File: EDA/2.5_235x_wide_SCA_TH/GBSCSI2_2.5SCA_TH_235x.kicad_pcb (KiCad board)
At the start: 4 copper layers, 69.5 x 93.5 mm, 145 parts, among them J1 SCSI_50-2P_2mm, J1.1 SCSI_50P_2.54mm, J2 TF003, J3 GCT-4105, J4 SM03B-SRSS-TB, J4.1 Conn_01x04, J5 Conn_01x04, J6 Conn_01x02, Q1 AO3401A, Q10 AO3401A, Q11 AO3401A, Q12 AO3401A, Q13 AO3401A, Q14 AO3401A, Q15 AO3401A, Q16 AO3401A, Q17 AO3401A, Q18 AO3401A, Q2 AO3401A, Q3 AO3401A, Q4 AO3401A, Q5 AO3401A, Q6 AO3401A, Q7 AO3401A, Q8 AO3401A, Q9 AO3401A, SW1 SW_DIP_x04, U1 RP2350_60QFN, U10 AZ1117-2.85, U2 W25Q128JVS, U3 USB TVS, U4 74LVTH245, U5 74LVTH245, U6 74LVTH125, U7 74LVTH125, U8 SN74AHC1G125DBVR, U9 TLV62569DBV, Y1 12MHz

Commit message: SCA variant mostly laid out
Or rather, a first pass.
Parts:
- removed C24, C32, C33: 100nF, Capacitor_SMD:C_0603_1608Metric
- removed C31, C34: 1μF, Capacitor_SMD:C_0603_1608Metric
- removed D1, D3, D4: 1N5819, Diode_SMD:D_SOD-123
- removed F1: 1A, Fuse:Fuse_0805_2012Metric
- removed J1.1: SCSI_50P_2.54mm, Connector_IDC:IDC-Header_2x25_P2.54mm_Horizontal
- removed J5: Conn_01x04, Connector_PinHeader_2.54mm:PinHeader_1x04_P2.54mm_Horizontal
- removed JP1: Jumper_2_Open, Connector_PinHeader_2.54mm:PinHeader_2x01_P2.54mm_Vertical
- removed Q1, Q10, Q11, Q12, Q13, Q14, Q15, Q16, Q17, Q18, Q2, Q3, Q4, Q5, Q6, Q7, Q8, Q9: AO3401A, Package_TO_SOT_SMD:SOT-23
- removed R11, R12, R29, R5, R7: 4.7kΩ, Resistor_SMD:R_0603_1608Metric
- removed R17, R27: 1kΩ, Resistor_SMD:R_0603_1608Metric
- removed R31, R32, R33, R34, R35, R36, R37, R38, R39, R40, R41, R42, R43, R44, R45, R46, R47, R48: 110Ω, Resistor_SMD:R_0603_1608Metric
- removed R52: 0Ω, Resistor_SMD:R_0603_1608Metric
- removed R53: ~, Resistor_SMD:R_0603_1608Metric
- removed SW1: SW_DIP_x04, Button_Switch_SMD:SW_DIP_SPSTx04_Slide_6.7x11.72mm_W8.61mm_P2.54mm_LowProfile
- removed U10: AZ1117-2.85, Package_TO_SOT_SMD:SOT-223-3_TabPin2
- removed U8: SN74AHC1G125DBVR, Package_TO_SOT_SMD:SOT-23-5
- added C15: 100nF, Capacitor_SMD:C_0402_1005Metric, F.Cu at (53.0, 110.8)
- added C36: 100nF, Capacitor_SMD:C_0402_1005Metric, F.Cu at (67.5, 111.8)
- added C37: 4.7μF, Capacitor_SMD:C_0402_1005Metric, F.Cu at (82.5, 97.1)
- added C38: 100nF, Capacitor_SMD:C_0402_1005Metric, F.Cu at (89.0, 100.2)
- added C39: 10μF, Capacitor_SMD:C_0603_1608Metric, F.Cu at (89.0, 103.2)
- added C40: 10μF, Capacitor_SMD:C_0603_1608Metric, F.Cu at (89.0, 101.8)
- added C41: 100nF, Capacitor_SMD:C_0603_1608Metric, F.Cu at (48.5, 84.5)
- added C42: 100nF, Capacitor_SMD:C_0402_1005Metric, F.Cu at (68.8, 79.5)
- added J8: Conn_01x02, Connector_PinHeader_2.54mm:PinHeader_1x02_P2.54mm_Vertical, F.Cu at (79.5, 116.2)
- added L3: 1μH, Inductor_SMD:L_1008_2520Metric, F.Cu at (89.2, 97.8)
- added R57: 4.7kΩ, Resistor_SMD:R_0603_1608Metric, F.Cu at (54.1, 84.5)
- added R58: 4.7kΩ, Resistor_SMD:R_0603_1608Metric, F.Cu at (84.0, 90.2)
- added R59: 4.7kΩ, Resistor_SMD:R_0603_1608Metric, F.Cu at (67.0, 84.5)
- added R60: 10kΩ, Resistor_SMD:R_0402_1005Metric, F.Cu at (86.0, 101.2)
- added R61: 374kΩ, Resistor_SMD:R_0402_1005Metric, F.Cu at (86.0, 103.2)
- added R62: 100kΩ, Resistor_SMD:R_0402_1005Metric, F.Cu at (86.0, 102.2)
- added R63: 10k, Resistor_SMD:R_0603_1608Metric, F.Cu at (53.2, 56.2)
- added R66: 4.7kΩ, Resistor_SMD:R_0603_1608Metric, F.Cu at (98.0, 140.5)
- added R67: 10k, Resistor_SMD:R_0603_1608Metric, F.Cu at (91.2, 56.2)
- added R68: 4.7kΩ, Resistor_SMD:R_0402_1005Metric, F.Cu at (49.5, 103.0)
- added R69: 4.7kΩ, Resistor_SMD:R_0402_1005Metric, F.Cu at (49.5, 105.0)
- added R70: 4.7kΩ, Resistor_SMD:R_0402_1005Metric, F.Cu at (49.5, 107.0)
- added SW2: SW_DIP_x03, Button_Switch_SMD:SW_DIP_SPSTx03_Slide_6.7x9.18mm_W8.61mm_P2.54mm_LowProfile, F.Cu at (96.2, 132.5)
- added SW3: GT-TC108A-H034-L1S, Button_Switch_SMD:SW_Push_1P1T-MP_NO_Horizontal_Alps_SKRTLAE010, F.Cu at (94.2, 140.5)
- added U11: TLV62569DBV, Package_TO_SOT_SMD:SOT-23-5, F.Cu at (85.2, 97.5)
- added U12: 74LVTH245, Package_SO:SSOP-20_5.3x7.2mm_P0.65mm, F.Cu at (45.2, 89.2)
- C10: value 4.7uF -> 4.7μF
- C20, C35: value 47uF -> 47μF
- J1: value SCSI_50-2P_2mm -> Conn_02x40_Counter_Clockwise; footprint GBSCSI:PinHeader_2x25-2_P2.00mm_straddle -> GBSCSI:CHAMPII_80; moved to B.Cu
- U1: value RP2350_60QFN -> RP2350_80QFN; footprint Package_DFN_QFN:QFN-60-1EP_7x7mm_P0.4mm_EP3.4x3.4mm_ThermalVias -> GBSCSI:RP2350-QFN-80-1EP_10x10_P0.4mm_EP3.4x3.4mm_ThermalVias
- moved D2 52.3 mm to (135.3, 96.8)
- moved F2 52.3 mm to (135.0, 99.1)
- moved REF** 38.8 mm to (56.5, 78.9)
- moved C20 17.7 mm to (80.0, 100.8), turned to 180 degrees
- moved C35 15.3 mm to (80.0, 103.2), turned to 180 degrees
- moved J1 13.8 mm to (70.3, 62.5), turned to 0 degrees
- moved R28 9.37 mm to (76.2, 84.5)
- moved R8 7.12 mm to (73.8, 85.2), turned to -90 degrees
- moved R30 7.04 mm to (73.8, 91.1)
- moved R25 6.64 mm to (84.0, 87.0)
- moved U4 6.57 mm to (56.5, 89.2)
- moved U6 6.57 mm to (69.0, 89.2)
- moved R26 6.55 mm to (95.4, 88.5)
- moved R6 6.55 mm to (96.0, 86.2)
- moved U5 6.55 mm to (89.8, 89.2)
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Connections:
- C22 pad 1: +3.3V -> +2.8V
- C23 pad 1: +3.3V -> +2.8V
- C25 pad 1: +3.3V -> +2.8V
- C26 pad 1: +3.3V -> +2.8V
- J1 pad 1: +5VIN -> unconnected-(J1-Pin_1-Pad1)
- J1 pad 10: /Host Interface/~{SCSI_SD2} -> /Host Interface/~{SCSI_SD8}
- J1 pad 11: GND -> /Host Interface/SCSI_I/~{O}
- J1 pad 12: /Host Interface/~{SCSI_SD3} -> /Host Interface/SCSI_~{REQ}
- J1 pad 13: GND -> /Host Interface/SCSI_~{C}/D
- J1 pad 14: /Host Interface/~{SCSI_SD4} -> /Host Interface/~{SCSI_SEL}
- J1 pad 15: GND -> /Host Interface/~{SCSI_MSG}
- J1 pad 16: /Host Interface/~{SCSI_SD5} -> /Host Interface/~{SCSI_RST}
- J1 pad 18: /Host Interface/~{SCSI_SD6} -> /Host Interface/~{SCSI_BSY}
- J1 pad 19: GND -> /Host Interface/SCSI_~{ATTN}
- J1 pad 2: +5VIN -> unconnected-(J1-Pin_2-Pad2)
- J1 pad 20: /Host Interface/~{SCSI_SD7} -> /Host Interface/~{SCSI_SDP}
- J1 pad 21: GND -> /Host Interface/~{SCSI_SD7}
- J1 pad 22: /Host Interface/~{SCSI_SDP} -> /Host Interface/~{SCSI_SD6}
- J1 pad 23: GND -> /Host Interface/~{SCSI_SD5}
- J1 pad 24: +5VTT -> /Host Interface/~{SCSI_SD4}
- J1 pad 25: /Host Interface/SCSI_~{ATTN} -> /Host Interface/~{SCSI_SD3}
- J1 pad 26: /Host Interface/~{SCSI_BSY} -> /Host Interface/~{SCSI_SD2}
- J1 pad 27: GND -> /Host Interface/~{SCSI_SD1}
- J1 pad 28: /Host Interface/~{SCSI_ACK} -> /Host Interface/~{SCSI_SD0}
- J1 pad 29: /Host Interface/~{SCSI_RST} -> /Host Interface/~{SCSI_SDP1}
- J1 pad 3: GND -> unconnected-(J1-Pin_3-Pad3)
- J1 pad 30: /Host Interface/~{SCSI_MSG} -> /Host Interface/~{SCSI_SD15}
- J1 pad 31: GND -> /Host Interface/~{SCSI_SD14}
- J1 pad 32: /Host Interface/~{SCSI_SEL} -> /Host Interface/~{SCSI_SD13}
- J1 pad 33: /Host Interface/SCSI_I/~{O} -> /Host Interface/~{SCSI_SD12}
- J1 pad 34: /Host Interface/SCSI_~{C}/D -> +5VIN
- J1 pad 35: GND -> +5VIN
- J1 pad 36: /Host Interface/SCSI_~{REQ} -> +5VIN
- J1 pad 37: GND -> unconnected-(J1-Pin_37-Pad37)
- J1 pad 38: GND -> unconnected-(J1-Pin_38-Pad38)
- J1 pad 39: +5VIN -> unconnected-(J1-Pin_39-Pad39)
- J1 pad 4: GND -> unconnected-(J1-Pin_4-Pad4)
- J1 pad 40: +5VIN -> unconnected-(J1-Pin_40-Pad40)
- J1 pad 43: unconnected-(J1-Pin_43-Pad43) -> GND
- J1 pad 44: unconnected-(J1-Pin_44-Pad44) -> Net-(J1-Pin_44)
- J1 pad 46: unconnected-(J1-Pin_46-Pad46) -> GND
- J1 pad 47: unconnected-(J1-Pin_47-Pad47) -> GND
- J1 pad 48: unconnected-(J1-Pin_48-Pad48) -> GND
- J1 pad 49: unconnected-(J1-Pin_49-Pad49) -> GND
- J1 pad 5: GND -> unconnected-(J1-Pin_5-Pad5)
- J1 pad 50: unconnected-(J1-Pin_50-Pad50) -> GND
- J1 pad 6: /Host Interface/~{SCSI_SD0} -> unconnected-(J1-Pin_6-Pad6)
- J1 pad 7: GND -> /Host Interface/~{SCSI_SD11}
- J1 pad 8: /Host Interface/~{SCSI_SD1} -> /Host Interface/~{SCSI_SD10}
- J1 pad 9: GND -> /Host Interface/~{SCSI_SD9}
- R10 pad 1: /Core Logic, Basic Controls/~{DEBUG} -> Net-(R10-Pad1)
- R10 pad 2: /Core Logic, Basic Controls/~{MCU_REQ} -> /Core Logic, Basic Controls/~{DEBUG}
- R13 pad 2: /Core Logic, Basic Controls/~{DEBUG} -> Net-(R10-Pad1)
- R6 pad 1: +3.3V -> +2.8V
- R8 pad 1: +3.3V -> +2.8V
- R9 pad 2: /Core Logic, Basic Controls/~{MCU_ATTN} -> /Core Logic, Basic Controls/~{MCU_ACK}
- U1 pad 1: +3.3V -> /Core Logic, Basic Controls/~{MCU_SD0}
- U1 pad 10: /Core Logic, Basic Controls/~{MCU_SD7} -> +1.1V
- U1 pad 11: +3.3V -> /Core Logic, Basic Controls/~{MCU_SD8}
- U1 pad 12: /Core Logic, Basic Controls/~{MCU_SDP} -> /Core Logic, Basic Controls/~{MCU_SD9}
- U1 pad 13: /Core Logic, Basic Controls/~{BUS_DIR} -> /Core Logic, Basic Controls/~{MCU_SD10}
- U1 pad 14: /Core Logic, Basic Controls/SDIO_CLK -> /Core Logic, Basic Controls/~{MCU_SD11}
- U1 pad 15: /Core Logic, Basic Controls/SDIO_CMD -> +3.3V
- U1 pad 16: /Core Logic, Basic Controls/SDIO_D0 -> /Core Logic, Basic Controls/~{MCU_SD12}
- U1 pad 17: /Core Logic, Basic Controls/SDIO_D1 -> /Core Logic, Basic Controls/~{MCU_SD13}
- U1 pad 18: /Core Logic, Basic Controls/SDIO_D2 -> /Core Logic, Basic Controls/~{MCU_SD14}
- U1 pad 19: /Core Logic, Basic Controls/SDIO_D3 -> /Core Logic, Basic Controls/~{MCU_SD15}
- U1 pad 2: /Core Logic, Basic Controls/~{MCU_SD0} -> /Core Logic, Basic Controls/~{MCU_SD1}
- U1 pad 20: +3.3V -> /Core Logic, Basic Controls/~{MCU_SDP}
- U1 pad 21: /Core Logic, Basic Controls/XIN -> /Core Logic, Basic Controls/~{MCU_SDP1}
- U1 pad 22: /Core Logic, Basic Controls/XOUT -> /Core Logic, Basic Controls/~{MCU_REQ}
- U1 pad 23: +1.1V -> /Core Logic, Basic Controls/BUS_DIR
- U1 pad 24: /Core Logic, Basic Controls/SWCLK -> +3.3V
- U1 pad 25: /Core Logic, Basic Controls/SWD -> /Core Logic, Basic Controls/~{MCU_CD/SEL_IN}
- U1 pad 26: unconnected-(U1-RUN-Pad26) -> /Core Logic, Basic Controls/~{MCU_ATTN}
- U1 pad 27: /Core Logic, Basic Controls/LED_OUT -> /Core Logic, Basic Controls/~{MCU_MSG/BSY_IN}
- U1 pad 28: /Core Logic, Basic Controls/~{MCU_REQ} -> /Core Logic, Basic Controls/~{MCU_ACK}
- U1 pad 29: /Core Logic, Basic Controls/~{MCU_CD/SEL_IN} -> +3.3V
- U1 pad 3: /Core Logic, Basic Controls/~{MCU_SD1} -> /Core Logic, Basic Controls/~{MCU_SD2}
- U1 pad 30: +3.3V -> /Core Logic, Basic Controls/XIN
- U1 pad 31: /Core Logic, Basic Controls/~{MCU_SEL_OUT} -> /Core Logic, Basic Controls/XOUT
- U1 pad 32: /Core Logic, Basic Controls/~{MCU_MSG/BSY_IN} -> +1.1V
- U1 pad 33: /Core Logic, Basic Controls/MCU_RST -> /Core Logic, Basic Controls/SWCLK
- U1 pad 34: /Core Logic, Basic Controls/~{MCU_IO} -> /Core Logic, Basic Controls/SWD
- U1 pad 35: /Core Logic, Basic Controls/~{WL_EN} -> unconnected-(U1-RUN-Pad35)
- U1 pad 36: /Core Logic, Basic Controls/WL_DAT/~{IRQ} -> /Core Logic, Basic Controls/~{MCU_IO}
- U1 pad 37: /Core Logic, Basic Controls/~{WL_CS} -> /Core Logic, Basic Controls/I²C_INT
- U1 pad 38: +3.3V -> /Core Logic, Basic Controls/I²C_SDA
- U1 pad 39: +1.1V -> /Core Logic, Basic Controls/I²C_SCL
- U1 pad 4: /Core Logic, Basic Controls/~{MCU_SD2} -> /Core Logic, Basic Controls/~{MCU_SD3}
- U1 pad 40: /Core Logic, Basic Controls/~{MCU_ACK} -> /Core Logic, Basic Controls/~{DEBUG}
- U1 pad 41: /Core Logic, Basic Controls/~{MCU_BSY_OUT} -> +3.3V
- U1 pad 42: /Core Logic, Basic Controls/~{MCU_ATTN} -> /Core Logic, Basic Controls/LED_OUT
- U1 pad 43: /Core Logic, Basic Controls/WL_SCK -> /Core Logic, Basic Controls/SDIO_CLK
- U1 pad 44: +3.3V -> /Core Logic, Basic Controls/SDIO_CMD
- U1 pad 45: +3.3V -> /Core Logic, Basic Controls/SDIO_D0
- U1 pad 46: Net-(U1-VREG_AVDD) -> /Core Logic, Basic Controls/SDIO_D1
- U1 pad 47: GND -> /Core Logic, Basic Controls/SDIO_D2
- U1 pad 48: /Core Logic, Basic Controls/VREG_LX -> /Core Logic, Basic Controls/SDIO_D3
- U1 pad 49: +3.3V -> /Core Logic, Basic Controls/~{WL_EN}
- U1 pad 5: /Core Logic, Basic Controls/~{MCU_SD3} -> +3.3V
- U1 pad 50: +1.1V -> +3.3V
- U1 pad 51: /Core Logic, Basic Controls/USB_D- -> +1.1V
- U1 pad 52: /Core Logic, Basic Controls/USB_D+ -> /Core Logic, Basic Controls/WL_DAT/~{IRQ}
- U1 pad 53: +3.3V -> /Core Logic, Basic Controls/~{WL_CS}
- U1 pad 54: +3.3V -> /Core Logic, Basic Controls/WL_SCK
- U1 pad 55: /Core Logic, Basic Controls/QSPI_SD3 -> /Core Logic, Basic Controls/EJECT
- U1 pad 56: /Core Logic, Basic Controls/QSPI_SCLK -> unconnected-(U1-GPIO45_ADC5-Pad56)
- U1 pad 57: /Core Logic, Basic Controls/QSPI_SD0 -> unconnected-(U1-GPIO46_ADC6-Pad57)
- U1 pad 58: /Core Logic, Basic Controls/QSPI_SD2 -> unconnected-(U1-GPIO47_ADC7-Pad58)
- U1 pad 59: /Core Logic, Basic Controls/QSPI_SD1 -> +3.3V
- U1 pad 6: +1.1V -> /Core Logic, Basic Controls/~{MCU_SD4}
- U1 pad 60: /Core Logic, Basic Controls/QSPI_~{SS} -> +3.3V
- U1 pad 61: GND -> Net-(U1-VREG_AVDD)
- U1 pad 7: /Core Logic, Basic Controls/~{MCU_SD4} -> /Core Logic, Basic Controls/~{MCU_SD5}
- U1 pad 8: /Core Logic, Basic Controls/~{MCU_SD5} -> /Core Logic, Basic Controls/~{MCU_SD6}
- U1 pad 9: /Core Logic, Basic Controls/~{MCU_SD6} -> /Core Logic, Basic Controls/~{MCU_SD7}
- U4 pad 1: /Core Logic, Basic Controls/~{BUS_DIR} -> /Core Logic, Basic Controls/BUS_DIR
- U4 pad 11: /Core Logic, Basic Controls/~{MCU_SD0} -> /Host Interface/~{SCSI_SD7}
- U4 pad 12: /Core Logic, Basic Controls/~{MCU_SD1} -> /Host Interface/~{SCSI_SD6}
- U4 pad 13: /Core Logic, Basic Controls/~{MCU_SD2} -> /Host Interface/~{SCSI_SD5}
- U4 pad 14: /Core Logic, Basic Controls/~{MCU_SD3} -> /Host Interface/~{SCSI_SD4}
- U4 pad 15: /Core Logic, Basic Controls/~{MCU_SD4} -> /Host Interface/~{SCSI_SD3}
- U4 pad 16: /Core Logic, Basic Controls/~{MCU_SD5} -> /Host Interface/~{SCSI_SD2}
- U4 pad 17: /Core Logic, Basic Controls/~{MCU_SD6} -> /Host Interface/~{SCSI_SD1}
- U4 pad 18: /Core Logic, Basic Controls/~{MCU_SD7} -> /Host Interface/~{SCSI_SD0}
- U4 pad 2: /Host Interface/~{SCSI_SD7} -> /Core Logic, Basic Controls/~{MCU_SD0}
- U4 pad 20: +3.3V -> +2.8V
- U4 pad 3: /Host Interface/~{SCSI_SD6} -> /Core Logic, Basic Controls/~{MCU_SD1}
- U4 pad 4: /Host Interface/~{SCSI_SD5} -> /Core Logic, Basic Controls/~{MCU_SD2}
- U4 pad 5: /Host Interface/~{SCSI_SD4} -> /Core Logic, Basic Controls/~{MCU_SD3}
- U4 pad 6: /Host Interface/~{SCSI_SD3} -> /Core Logic, Basic Controls/~{MCU_SD4}
- U4 pad 7: /Host Interface/~{SCSI_SD2} -> /Core Logic, Basic Controls/~{MCU_SD5}
- U4 pad 8: /Host Interface/~{SCSI_SD1} -> /Core Logic, Basic Controls/~{MCU_SD6}
- U4 pad 9: /Host Interface/~{SCSI_SD0} -> /Core Logic, Basic Controls/~{MCU_SD7}
- U5 pad 20: +3.3V -> +2.8V
- U6 pad 1: /Core Logic, Basic Controls/~{BUS_DIR} -> /Core Logic, Basic Controls/~{MCU_RST_OUT}
- U6 pad 14: +3.3V -> +2.8V
- U6 pad 2: /Core Logic, Basic Controls/~{MCU_SDP} -> GND
- U6 pad 3: /Host Interface/~{SCSI_SDP} -> /Host Interface/~{SCSI_RST}
- U6 pad 5: /Host Interface/~{SCSI_SDP} -> /Host Interface/~{SCSI_RST}
- U6 pad 6: Net-(R27-Pad1) -> /Core Logic, Basic Controls/~{MCU_RST_IN}
- U7 pad 1: /Core Logic, Basic Controls/~{MCU_SEL_OUT} -> GND
- U7 pad 10: /SCSI Buffers/~{RST_OUT} -> GND
- U7 pad 11: Net-(R29-Pad1) -> unconnected-(U7-Pad11)
- U7 pad 12: /Host Interface/~{SCSI_RST} -> GND
- U7 pad 14: +3.3V -> +2.8V
- U7 pad 2: GND -> /Host Interface/~{SCSI_SEL}
- U7 pad 3: /Host Interface/~{SCSI_SEL} -> Net-(R28-Pad2)
- U7 pad 4: GND -> /Core Logic, Basic Controls/~{MCU_SEL_OUT}
- U7 pad 5: /Host Interface/~{SCSI_SEL} -> GND
- U7 pad 6: Net-(R28-Pad2) -> /Host Interface/~{SCSI_SEL}
- U7 pad 8: /Host Interface/~{SCSI_RST} -> unconnected-(U7-Pad8)
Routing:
- net +2.8V: track 192.9 -> 21.2 mm, vias 21 -> 13
- net +5VIN: track 200.9 -> 38.1 mm, vias 8 -> 0
- net /Core Logic, Basic Controls/~{TERM_EN}: track 151.1 -> 0.00 mm, vias 18 -> 0
- net VBUS: track 111.5 -> 20.3 mm
- net /Core Logic, Basic Controls/~{MCU_REQ}: track 125.2 -> 48.7 mm, vias 5 -> 2
- net /Host Interface/~{SCSI_SD10}: track 0.00 -> 70.0 mm, vias 0 -> 1
- net /Core Logic, Basic Controls/MCU_RST: track 68.7 -> 0.00 mm, vias 4 -> 0
- net /Host Interface/~{SCSI_SD8}: track 0.00 -> 68.3 mm, vias 0 -> 1
- net /Core Logic, Basic Controls/~{MCU_IO}: track 122.8 -> 54.5 mm, vias 5 -> 2
- net /Host Interface/~{SCSI_SD11}: track 0.00 -> 67.0 mm, vias 0 -> 1
- net /Host Interface/~{SCSI_SD9}: track 0.00 -> 65.3 mm, vias 0 -> 1
- net /Core Logic, Basic Controls/EJECT: track 0.00 -> 57.1 mm, vias 0 -> 1
- net /Core Logic, Basic Controls/~{MCU_ATTN}: track 108.9 -> 54.0 mm, vias 5 -> 2
- net +5VTT: track 53.1 -> 0.00 mm
- net /Core Logic, Basic Controls/BUS_DIR: track 0.00 -> 51.7 mm, vias 0 -> 2
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- added copper zone on F.Cu, net +2.8V
- removed copper zone on F.Cu, net +5VIN
- removed copper zone on F.Cu, net Net-(U10-GND)
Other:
- board text added: "1A"
- board text added: "2.5{dblquote} RP235x Wide SCA pcb v2.0"
- board text removed: "2.5{dblquote} RP235x Narrow pcb v2.0"
- board text removed: "GBSCSI2"
- board text removed: "TERMPWR"
- board text removed: "Term."

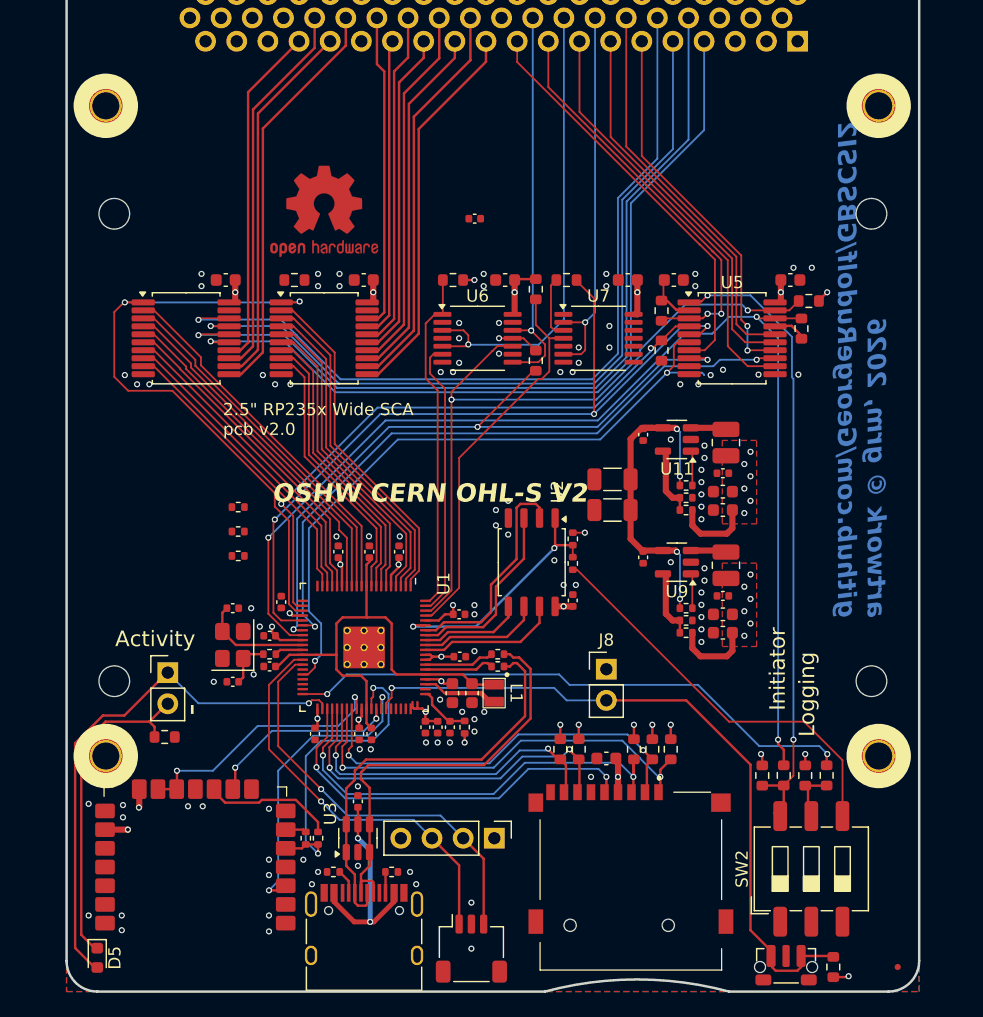
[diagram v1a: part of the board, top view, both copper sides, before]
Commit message: Tidying up PCB footprint slightly, more work needed, ERC passes on narrow variants
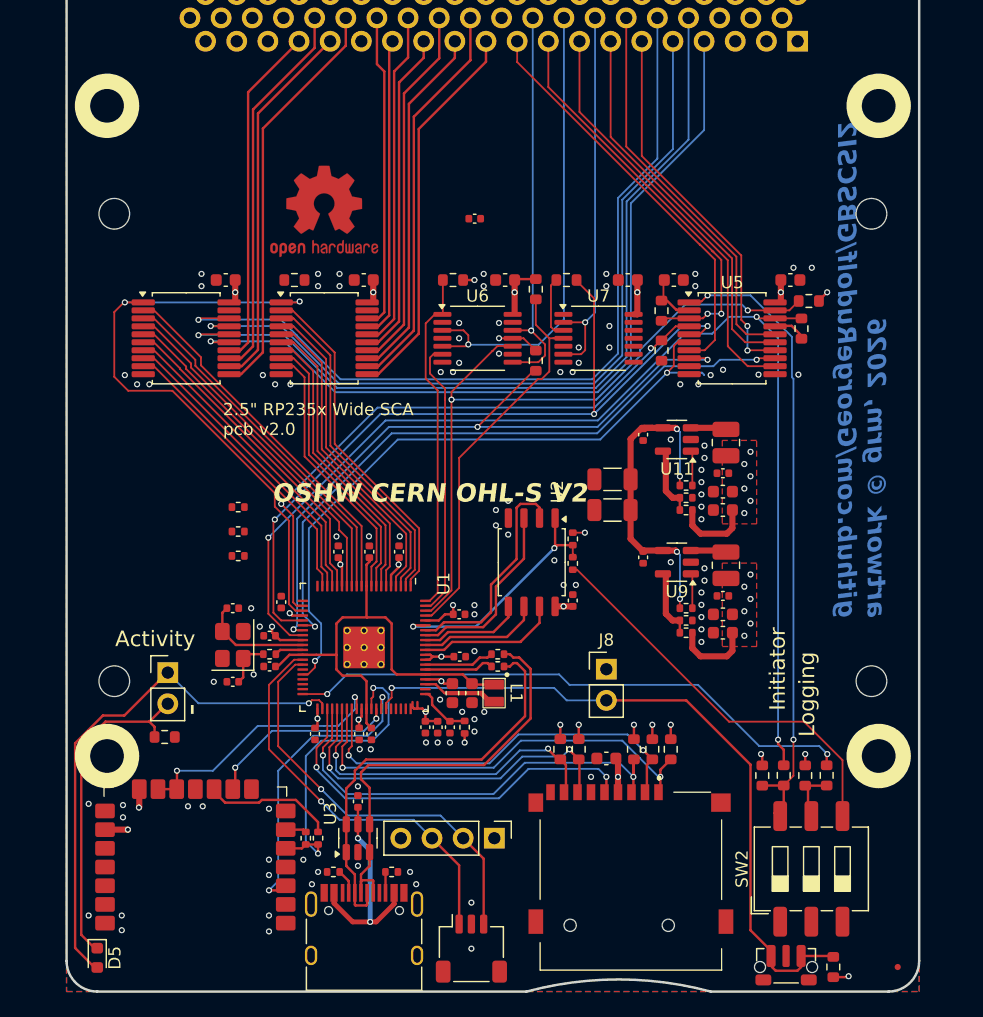
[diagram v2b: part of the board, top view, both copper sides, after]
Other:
- outline, holes or cut-outs redrawn

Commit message: Prettifying models
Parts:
- removed the C15 at (53.0, 110.8)
- added C43: 100nF, Capacitor_SMD:C_0402_1005Metric, F.Cu at (67.5, 104.8)
- added D4: 1N5819, Diode_SMD:D_SOD-123, F.Cu at (83.0, 104.5)
- added J7: Conn_01x05, Connector_PinSocket_2.54mm:PinSocket_1x05_P2.54mm_Vertical, F.Cu at (43.8, 92.2)
- moved D2 55.3 mm to (80.5, 104.5), turned to -90 degrees
- moved F2 54.5 mm to (80.5, 99.8), turned to 90 degrees
- moved C36 16.6 mm to (53.0, 103.8), turned to 90 degrees
- moved R68 8.78 mm to (46.5, 94.8)
- moved R69 8.31 mm to (46.5, 97.2)
- moved C1 7.00 mm to (67.0, 111.2)
- moved C10 7.00 mm to (60.4, 114.5)
- moved C11 7.00 mm to (52.0, 109.0)
- moved C13 7.00 mm to (62.6, 99.7)
- moved C14 7.00 mm to (57.6, 99.7)
- moved C15 7.00 mm to (52.0, 106.5)
- moved C16 7.00 mm to (55.8, 114.5)
- moved C17 7.00 mm to (59.4, 114.5)
- moved C19 7.00 mm to (67.5, 108.2)
- moved C2 7.00 mm to (49.0, 104.2)
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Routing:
- net +5VIN: track 38.1 -> 137.8 mm, vias 0 -> 2
- net VBUS: track 20.5 -> 56.8 mm, vias 4 -> 5
- net /Core Logic, Basic Controls/I²C_SCL: track 0.00 -> 28.7 mm, vias 0 -> 1
- net /Core Logic, Basic Controls/I²C_SDA: track 0.00 -> 28.4 mm, vias 0 -> 1
- net /Core Logic, Basic Controls/I²C_INT: track 0.00 -> 22.3 mm, vias 0 -> 2
- net /Core Logic, Basic Controls/~{INITIATOR}: track 51.8 -> 65.2 mm
- net +3.3V: track 62.4 -> 53.1 mm, vias 30 -> 32
- net /Core Logic, Basic Controls/~{USB_BOOT}: track 33.0 -> 39.5 mm
- net /Power/5V_TIE: track 4.96 -> 1.56 mm
- net /Core Logic, Basic Controls/~{MCU_IO}: track 54.5 -> 51.4 mm
- net +2.8V: track 21.2 -> 24.2 mm, vias 13 -> 14
- net /Core Logic, Basic Controls/~{MCU_ACK}: track 98.2 -> 100.8 mm, vias 3 -> 4
- net +5V: track 30.7 -> 28.3 mm
- net /Core Logic, Basic Controls/BUS_DIR: track 51.7 -> 53.6 mm
- net Net-(R30-Pad2): track 3.41 -> 2.30 mm, vias 1 -> 0
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- added copper zone on B.Cu, net +2.8V
- added copper zone on B.Cu, net +3.3V
- added copper zone on B.Cu, net +5VIN
- added copper zone on F.Cu, net +5VIN
- added copper zone on In1.Cu, net +5VIN
- added copper zone on In2.Cu, net +5VIN
- added copper zone on In2.Cu, net GND
- removed copper zone on In2.Cu, net +3.3V
- removed copper zone on B.Cu, net GND
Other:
- board text added: "3.3V"
- board text added: "EJECT"
- board text added: "GND"
- board text added: "SCL"
- board text added: "SDA"
- board text added: "SWC"
- board text added: "SWD"
- board text added: "USB Boot"

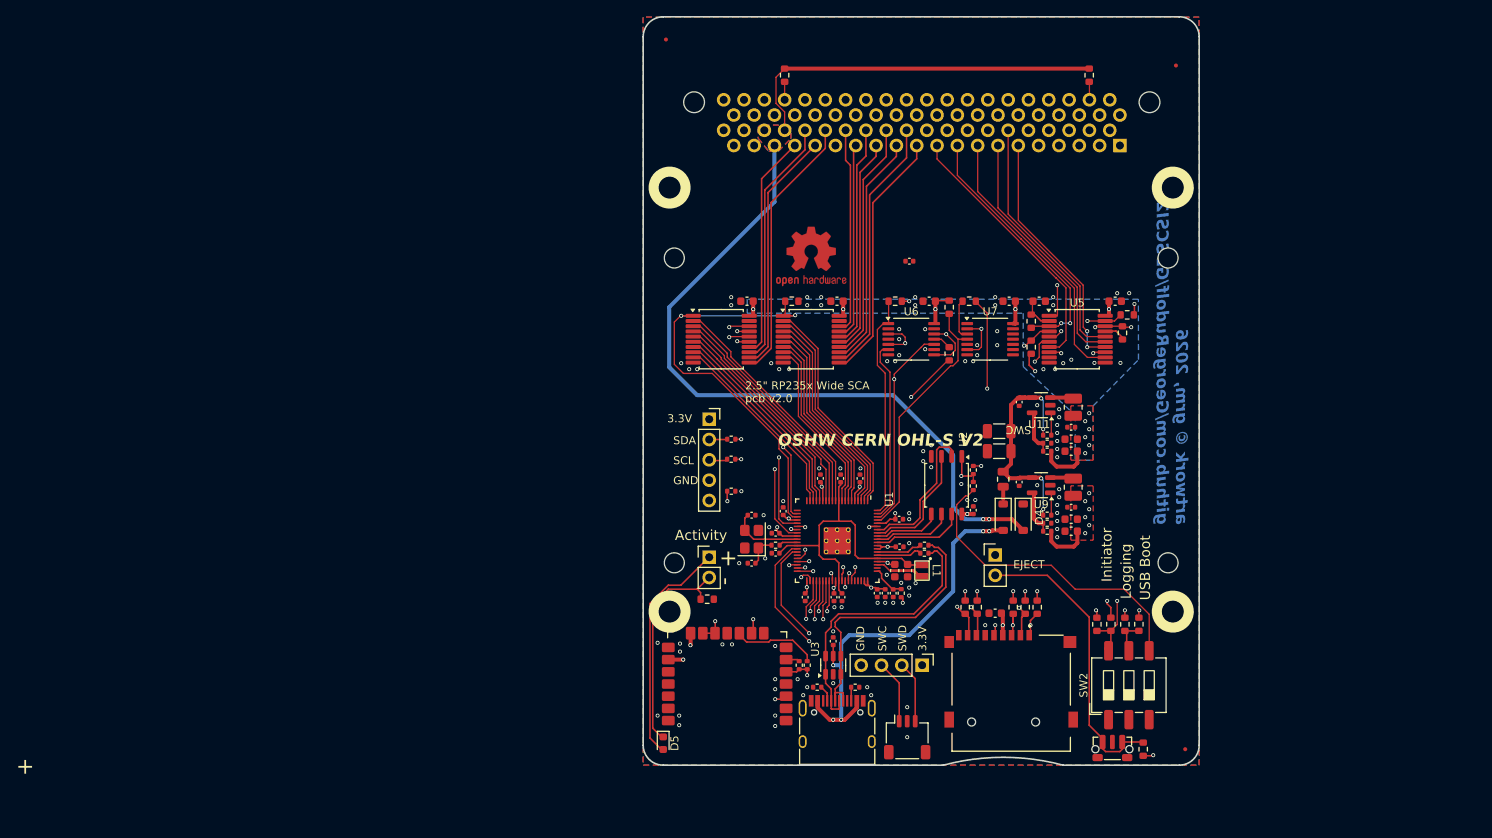
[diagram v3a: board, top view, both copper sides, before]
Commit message: Fixing PCB footprint
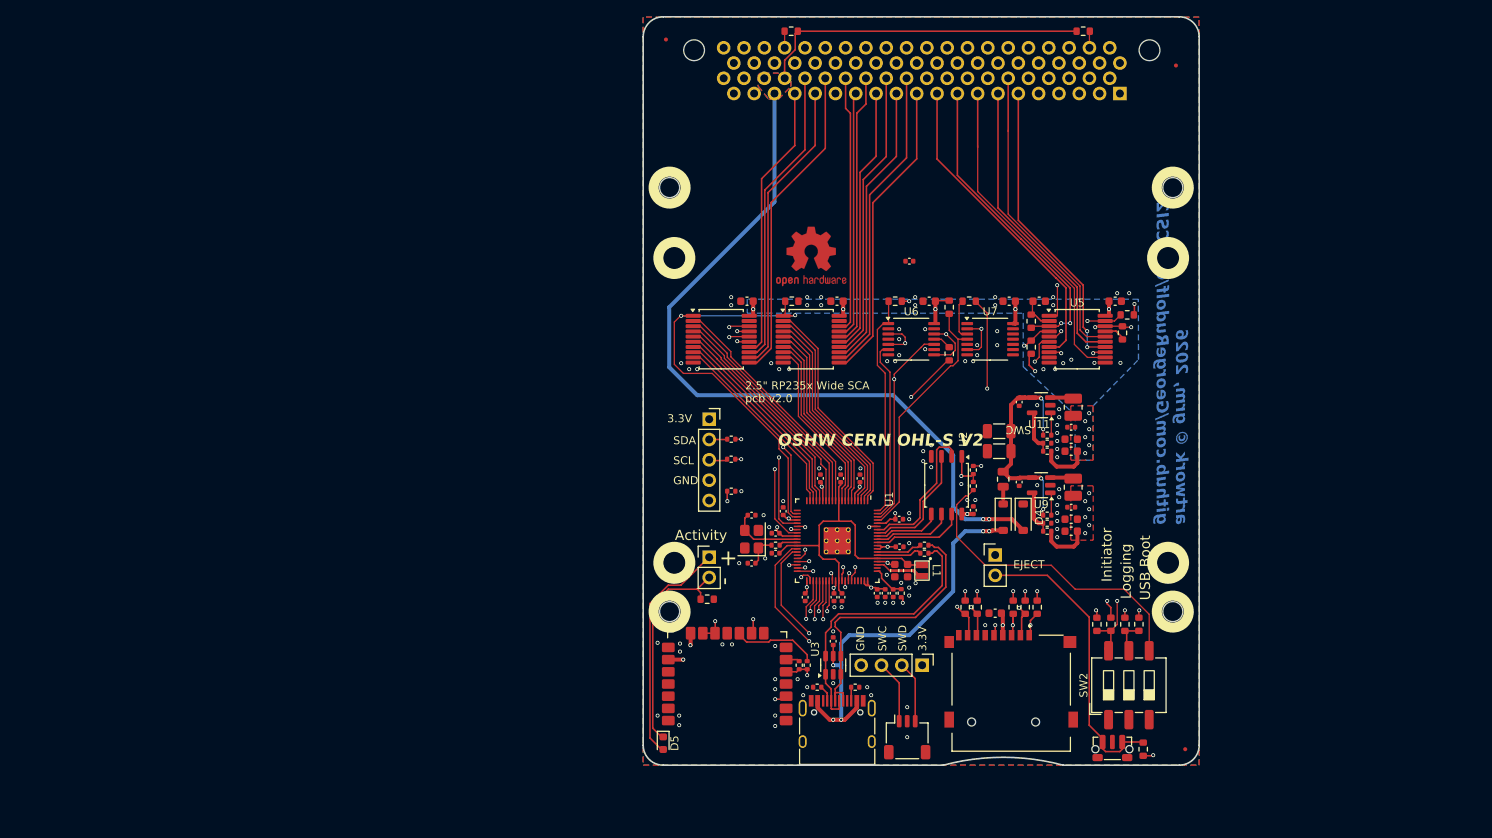
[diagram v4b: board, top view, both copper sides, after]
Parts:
- moved J1 6.50 mm to (70.3, 49.0)
- moved R63 5.56 mm to (54.0, 43.8), turned to 0 degrees
- moved R67 5.55 mm to (90.5, 43.8), turned to 180 degrees
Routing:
- net /Host Interface/~{SCSI_MSG}: track 34.4 -> 41.1 mm
- net /Host Interface/~{SCSI_SD8}: track 68.3 -> 75.0 mm
- net /Host Interface/SCSI_~{REQ}: track 32.2 -> 38.8 mm
- net /Host Interface/~{SCSI_SD9}: track 65.3 -> 71.8 mm
- net /Host Interface/~{SCSI_SD11}: track 67.0 -> 73.5 mm
- net /Host Interface/~{SCSI_RST}: track 38.4 -> 44.9 mm
- net /Host Interface/~{SCSI_SD5}: track 29.3 -> 35.8 mm
- net /Host Interface/~{SCSI_SD14}: track 30.5 -> 37.0 mm
- net /Host Interface/~{SCSI_SD12}: track 28.1 -> 34.6 mm
- net /Host Interface/SCSI_I/~{O}: track 31.0 -> 37.5 mm
- net /Host Interface/~{SCSI_SEL}: track 31.1 -> 37.6 mm
- net /Host Interface/~{SCSI_SD6}: track 32.4 -> 38.9 mm
- net /Host Interface/~{SCSI_SD3}: track 27.0 -> 33.5 mm
- net /Host Interface/~{SCSI_SD2}: track 27.7 -> 34.2 mm
- net /Host Interface/~{SCSI_SD1}: track 24.6 -> 31.1 mm
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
